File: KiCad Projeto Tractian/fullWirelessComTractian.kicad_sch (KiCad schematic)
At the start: 34 parts, among them SW1 ResetButton, U1 ESP8266EX, U2 ATmega328P-A, U3 TXB0108DQSR, U4 MX25R3235FM2xx1, U5 AMS1117-3.3, U6 AMS1117-5.0, Y1 16MHz, Y2 XTAL 16Mhz ±10ppm (TSX -3225 )

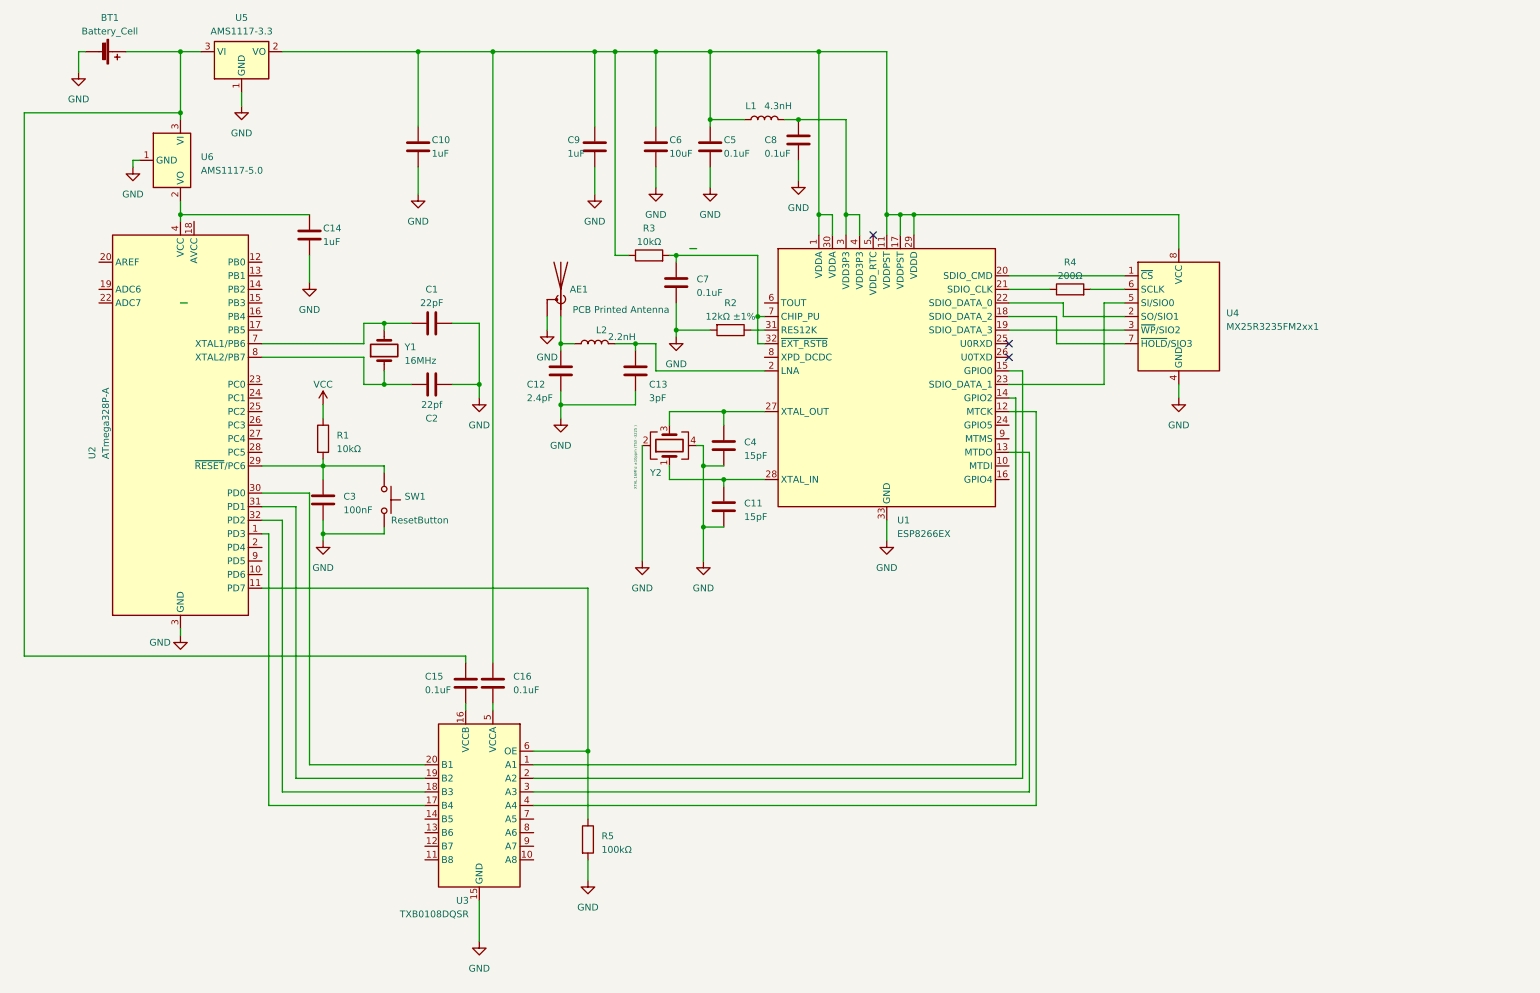
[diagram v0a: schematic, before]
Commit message: 1 - :fire: | 2 -:memo: | 1 - Remocao dos circuitos p/ Atmega328P-A e Alimentacao Rede | 2 - Add Data Sheet AMS1117
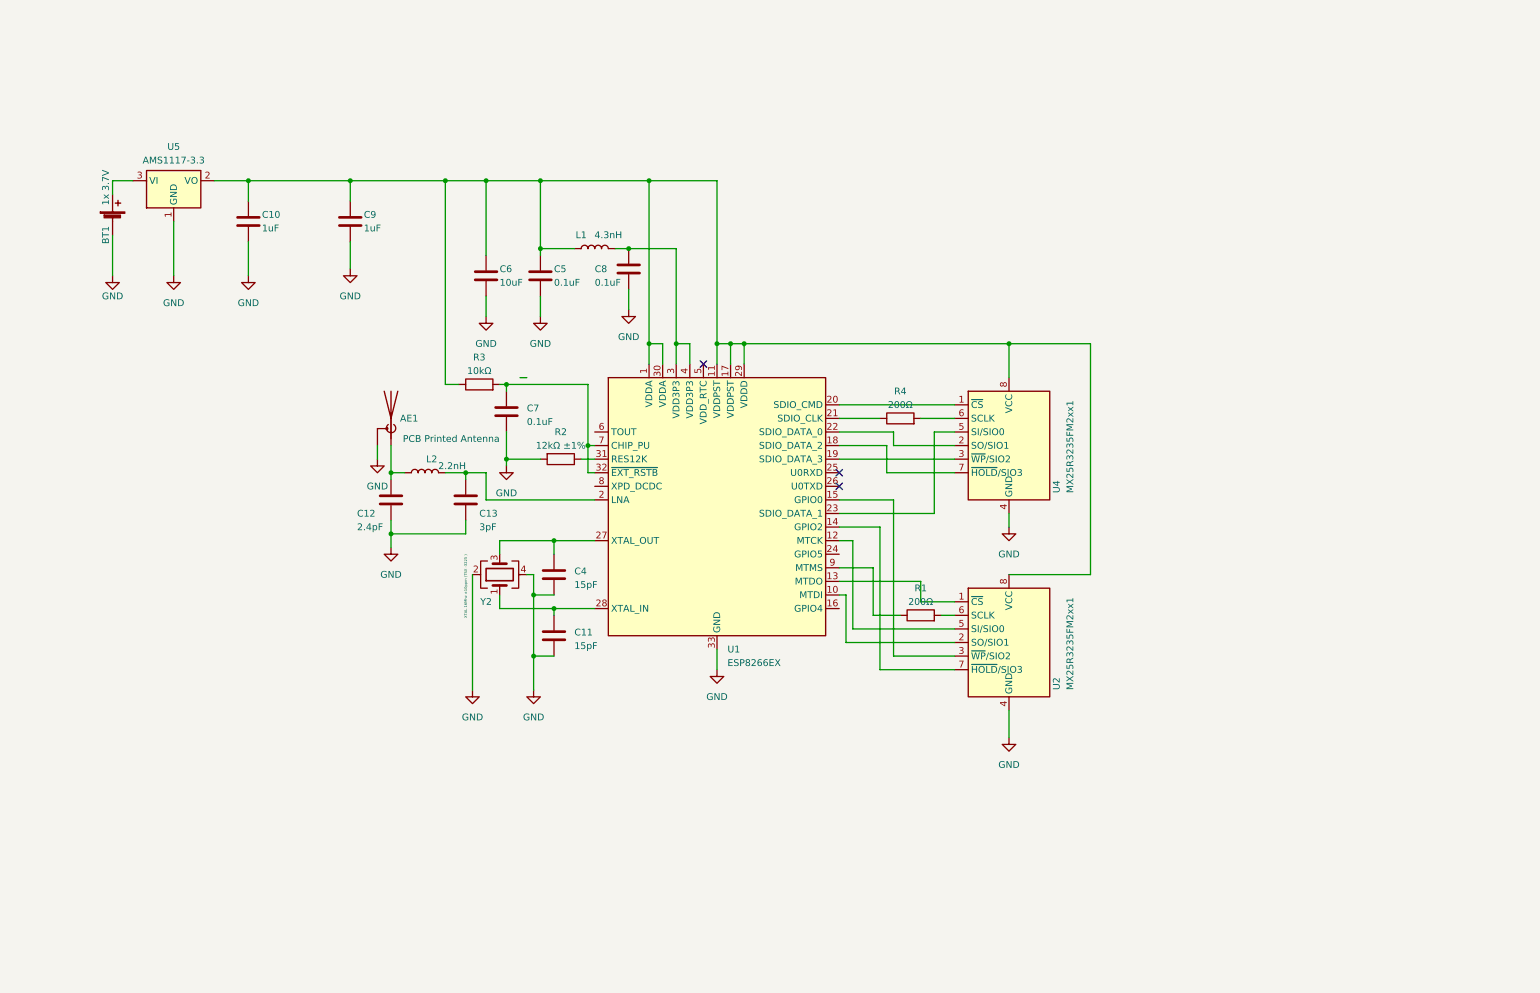
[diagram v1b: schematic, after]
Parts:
- removed C1: 22pF, Capacitor_SMD:C_0201_0603Metric_Pad0.64x0.40mm_HandSolder, symbol Device:C
- removed C14: 1uF, Capacitor_SMD:C_0201_0603Metric_Pad0.64x0.40mm_HandSolder, symbol Device:C
- removed C15, C16: 0.1uF, Capacitor_SMD:C_0201_0603Metric_Pad0.64x0.40mm_HandSolder, symbol Device:C
- removed C2: 22pf, Capacitor_SMD:C_0201_0603Metric_Pad0.64x0.40mm_HandSolder, symbol Device:C
- removed C3: 100nF, Capacitor_SMD:C_0201_0603Metric_Pad0.64x0.40mm_HandSolder, symbol Device:C
- removed R5: 100kΩ, Resistor_SMD:R_0201_0603Metric_Pad0.64x0.40mm_HandSolder, symbol Device:R
- removed SW1: ResetButton, Button_Switch_THT:SW_Tactile_Straight_KSA0Axx1LFTR, symbol Switch:SW_MEC_5G
- removed U2: ATmega328P-A, Package_QFP:TQFP-32_7x7mm_P0.8mm, symbol MCU_Microchip_ATmega:ATmega328P-A
- removed U3: TXB0108DQSR, Package_SON:USON-20_2x4mm_P0.4mm, symbol Logic_LevelTranslator:TXB0108DQSR
- removed U6: AMS1117-5.0, Package_TO_SOT_SMD:SOT-223-3_TabPin2, symbol Regulator_Linear:AMS1117-5.0
- removed Y1: 16MHz, Crystal:Crystal_HC52-6mm_Vertical, symbol Device:Crystal
- added U2: MX25R3235FM2xx1, Package_SO:SOP-8_5.28x5.23mm_P1.27mm, symbol Memory_Flash:MX25R3235FM2xx1
- BT1: value Battery_Cell -> 1x 3.7V; footprint Battery:BatteryHolder_ComfortableElectronic_CH273-2450_1x2450 -> Battery:BatteryHolder_Keystone_2466_1xAAA
- R1: value 10kΩ -> 200Ω; footprint Resistor_SMD:R_0201_0603Metric_Pad0.64x0.40mm_HandSolder -> Resistor_SMD:R_0402_1005Metric_Pad0.72x0.64mm_HandSolder
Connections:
- net VCC is gone; now on an unnamed net: R1.1
- net GND: now also U2.4 (GND)
- net at R1.2: now also U2.6 (SCLK)
- net at C10.1, C5.1, C6.1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: now also U2.8 (VCC)
- net at U1.14 (GPIO2): now also U2.7 (~{HOLD}/SIO3)
- net at U1.15 (GPIO0): now also U2.3 (~{WP}/SIO2)
- net at U1.13 (MTDO): now also U2.1 (~{CS})
- net at U1.12 (MTCK): now also U2.5 (SI/SIO0)
- net at U1.10 (MTDI): now also U2.2 (SO/SIO1)
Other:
- moved on the sheet: AE1, BT1, C10, C11, C12, C13, C4, C5, C6, C7, C8, C9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

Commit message: :construction: Arranjo dos componentes | destaque para o circuito pi e XTAL em 0.8mm
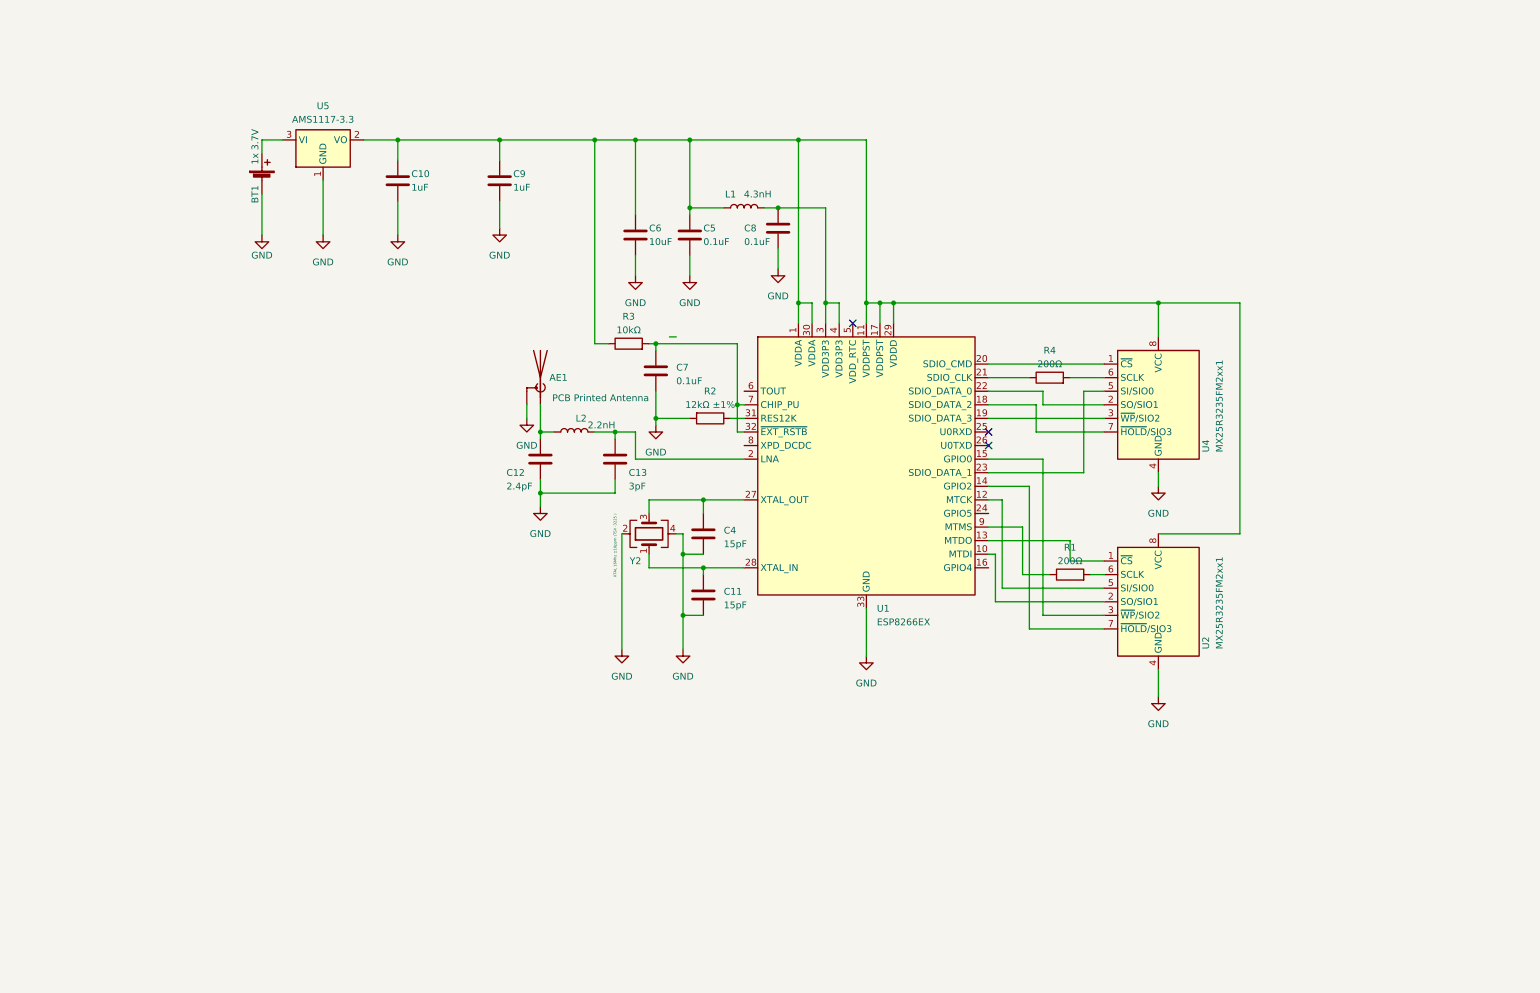
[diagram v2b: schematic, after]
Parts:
- Y2: footprint Oscillator:Oscillator_SMD_SeikoEpson_SG8002CE-4Pin_3.2x2.5mm_HandSoldering -> Oscillator:Oscillator_SMD_SeikoEpson_SG210-4Pin_2.5x2.0mm_HandSoldering
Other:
- moved on the sheet: AE1, BT1, C10, C11, C12, C13, C4, C5, C6, C7, C8, C9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

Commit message: :construction: Schematics reorganizado | definicao de trail mils para power/GND lines e signal lines
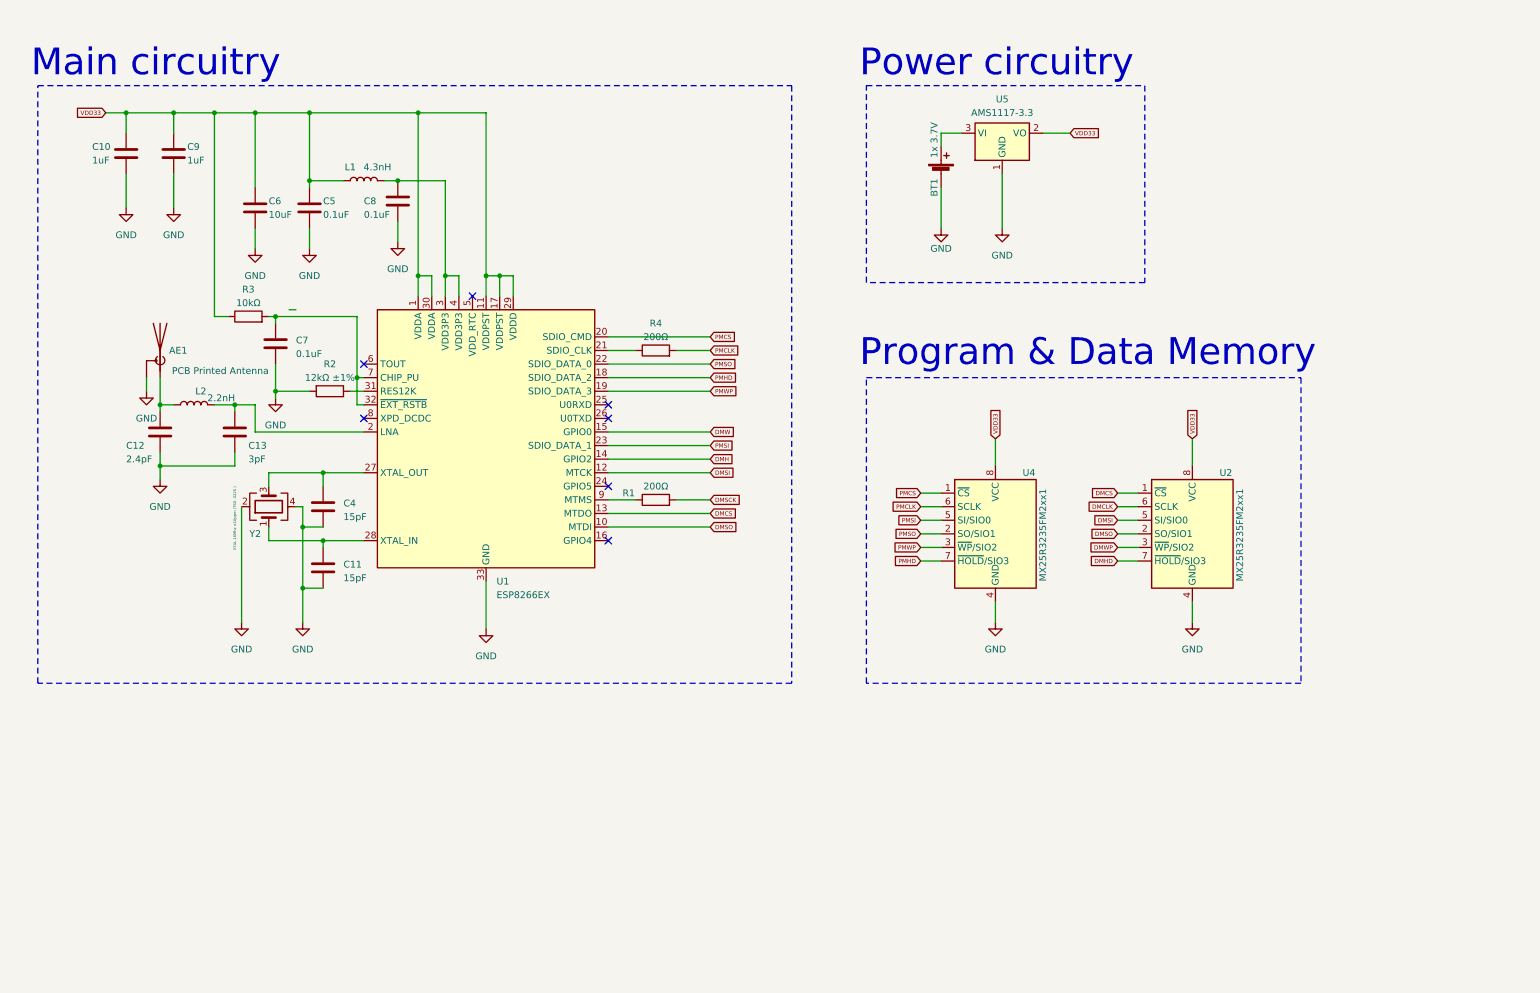
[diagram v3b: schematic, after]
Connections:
- net DMCLK: now reaches U2.6 (SCLK)
- net DMCLK: no longer R1.2
- net VDD33: now reaches C10.1, C5.1, C6.1, C9.1, L1.1, R3.1, U1.1 (VDDA), U1.11 (VDDPST), U1.17 (VDDPST), U1.29 (VDDD), U1.30 (VDDA), U2.8 (VCC), U4.8 (VCC), U5.2 (VO)
- net PMCS: now reaches U1.20 (SDIO_CMD), U4.1 (~{CS})
- net PMSO: now reaches U1.22 (SDIO_DATA_0), U4.2 (SO/SIO1)
- net PMWP: now reaches U1.19 (SDIO_DATA_3), U4.3 (~{WP}/SIO2)
- net PMSI: now reaches U1.23 (SDIO_DATA_1), U4.5 (SI/SIO0)
- net PMCLK: now reaches R4.2, U4.6 (SCLK)
- net PMHD: now reaches U1.18 (SDIO_DATA_2), U4.7 (~{HOLD}/SIO3)
- net DMCS: now reaches U1.13 (MTDO), U2.1 (~{CS})
- net DMSO: now reaches U1.10 (MTDI), U2.2 (SO/SIO1)
- net DMW: now reaches U1.15 (GPIO0)
- net DMW: no longer U2.3 (~{WP}/SIO2)
- net DMSI: now reaches U1.12 (MTCK), U2.5 (SI/SIO0)
- net DMH: now reaches U1.14 (GPIO2)
- net DMH: no longer U2.7 (~{HOLD}/SIO3)
- new net DMHD: U2.7 (~{HOLD}/SIO3)
- new net DMSCK: R1.2
- new net DMWP: U2.3 (~{WP}/SIO2)
- no-connect marks 3 -> 7
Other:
- note added: "Main circuitry"
- note added: "Power circuitry"
- note added: "Program & Data Memory"
- moved on the sheet: AE1, BT1, C10, C11, C12, C13, C4, C5, C6, C7, C8, C9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

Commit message: 1 - :boom: | 2 - :memo: | 1- Calculo e projeto da impedancia de 50ohms para a antena RF | 2 - add datasheet antena RTexasSWRA117D 2.4GHz
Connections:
- net DMSCK is gone; now on net DMCLK: R1.2
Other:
- moved on the sheet: AE1

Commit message: :construction: Nova organizacao da PCB | Routing in progress
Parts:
- added C1: 0.1uF, Capacitor_SMD:C_0201_0603Metric_Pad0.64x0.40mm_HandSolder, symbol Device:C
- added C2: 2.2uF, Capacitor_Tantalum_SMD:CP_EIA-1608-08_AVX-J_Pad1.25x1.05mm_HandSolder, symbol Device:C_Polarized
- added R5: 220kΩ ±1%, Resistor_SMD:R_0201_0603Metric_Pad0.64x0.40mm_HandSolder, symbol Device:R
- added R6: 100kΩ ±1%, Resistor_SMD:R_0201_0603Metric_Pad0.64x0.40mm_HandSolder, symbol Device:R
- added U6: TMP36xS, Package_SO:SOIC-8_3.9x4.9mm_P1.27mm, symbol Sensor_Temperature:TMP36xS
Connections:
- net GND: now also C1.2, C2.2, R6.2, U6.4 (GND)
- net VDD33: now also C1.1, C2.1, U6.8 (+Vs)
- net TMPSD: now reaches U1.24 (GPIO5)
- net TMPSD: now also U6.5 (~{SHUTDOWN})
- net TOUT: now reaches U1.6 (TOUT)
- net TOUT: now also R5.2, R6.1
- new net: R5.1, U6.1 (V_{OUT})
- no-connect marks 7 -> 5
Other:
- note added: "Temp. Sensor Circuitry"
- moved on the sheet: AE1, BT1, C10, C11, C12, C13, C4, C5, C6, C7, C8, C9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

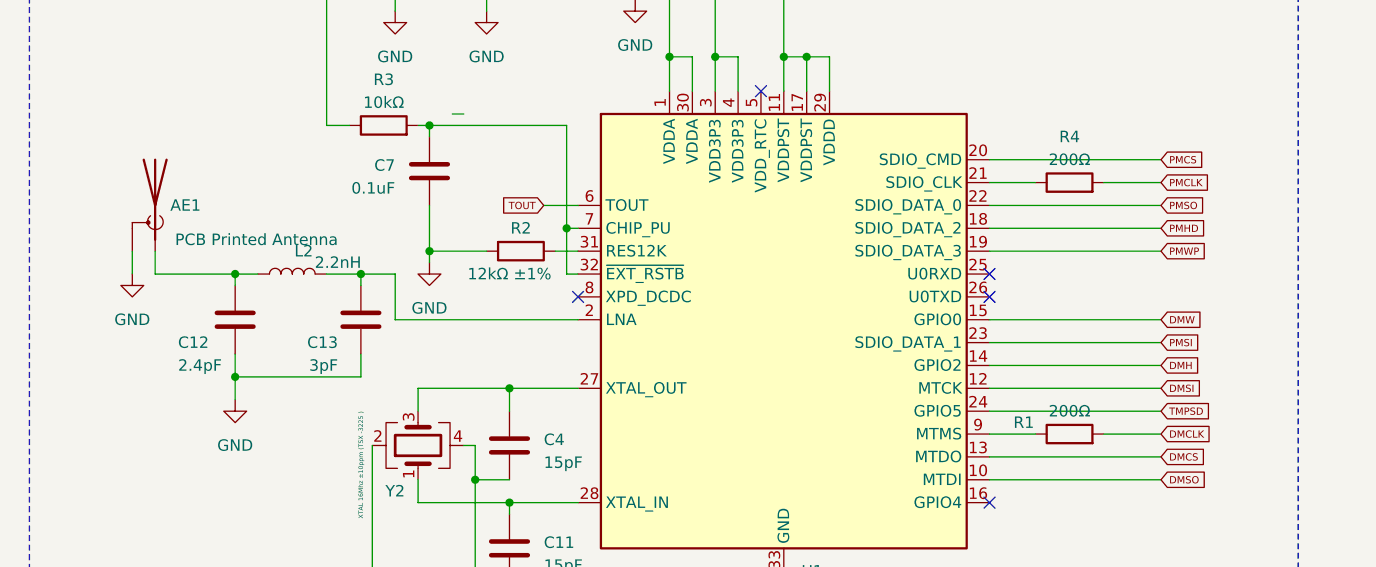
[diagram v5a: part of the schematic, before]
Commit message: :construction: PCB Routes Finished | PCB Borders defined | ANT1 track drawn manually (error ignore on no net connection for ANT1)
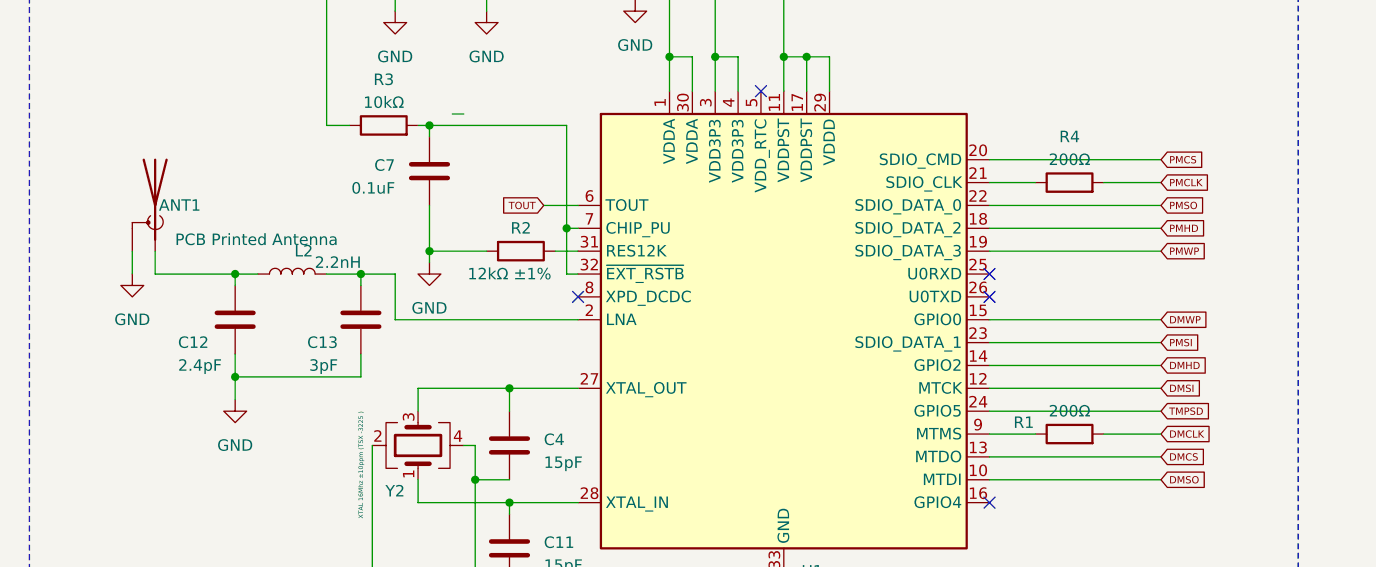
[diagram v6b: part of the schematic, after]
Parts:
- renumbered AE1 to ANT1
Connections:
- net DMH is gone; now on net DMHD: U1.14 (GPIO2)
- net DMW is gone; now on net DMWP: U1.15 (GPIO0)
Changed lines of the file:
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@@
     )
   )
-  (global_label "DMH" (shape input) (at 142.24 152.4 0) (fields_autoplaced)
-    (effects (font (size 0.8 0.8)) (justify left))
-    (property "Intersheetrefs" "${INTERSHEET_REFS}" (at 146.6227 152.4 0)
+  (global_label "DMHD" (shape input) (at 142.24 152.4 0) (fields_autoplaced)
+    (effects (font (size 0.8 0.8)) (justify left))
+    (property "Intersheetrefs" "${INTERSHEET_REFS}" (at 147.4227 152.4 0)
       (effects (font (size 1.27 1.27)) (justify left) hide)
     )
@@
     )
   )
-  (global_label "DMW" (shape input) (at 142.24 147.32 0) (fields_autoplaced)
-    (effects (font (size 0.8 0.8)) (justify left))
-    (property "Intersheetrefs" "${INTERSHEET_REFS}" (at 146.6989 147.32 0)
+  (global_label "DMWP" (shape input) (at 142.24 147.32 0) (fields_autoplaced)
+    (effects (font (size 0.8 0.8)) (justify left))
+    (property "Intersheetrefs" "${INTERSHEET_REFS}" (at 147.4989 147.32 0)
       (effects (font (size 1.27 1.27)) (justify left) hide)
     )
@@
   (symbol (lib_id "Device:Antenna_Shield") (at 30.48 134.62 0) (mirror y) (unit 1)
     (in_bom yes) (on_board yes) (dnp no)
-    (property "Reference" "AE1" (at 35.56 134.62 0)
+    (property "Reference" "ANT1" (at 35.56 134.62 0)
       (effects (font (size 1.27 1.27)) (justify left))
     )
@@
       (project "fullWirelessComTractian"
         (path "/de37416f-2273-481a-bd7e-d92c2e99b78a"
-          (reference "AE1") (unit 1)
-        )
-      )
+          (reference "ANT1") (unit 1)
+        )
+      )
